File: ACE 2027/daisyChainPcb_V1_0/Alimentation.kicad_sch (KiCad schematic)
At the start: 3 parts, among them U2 AP7361C-33E-13

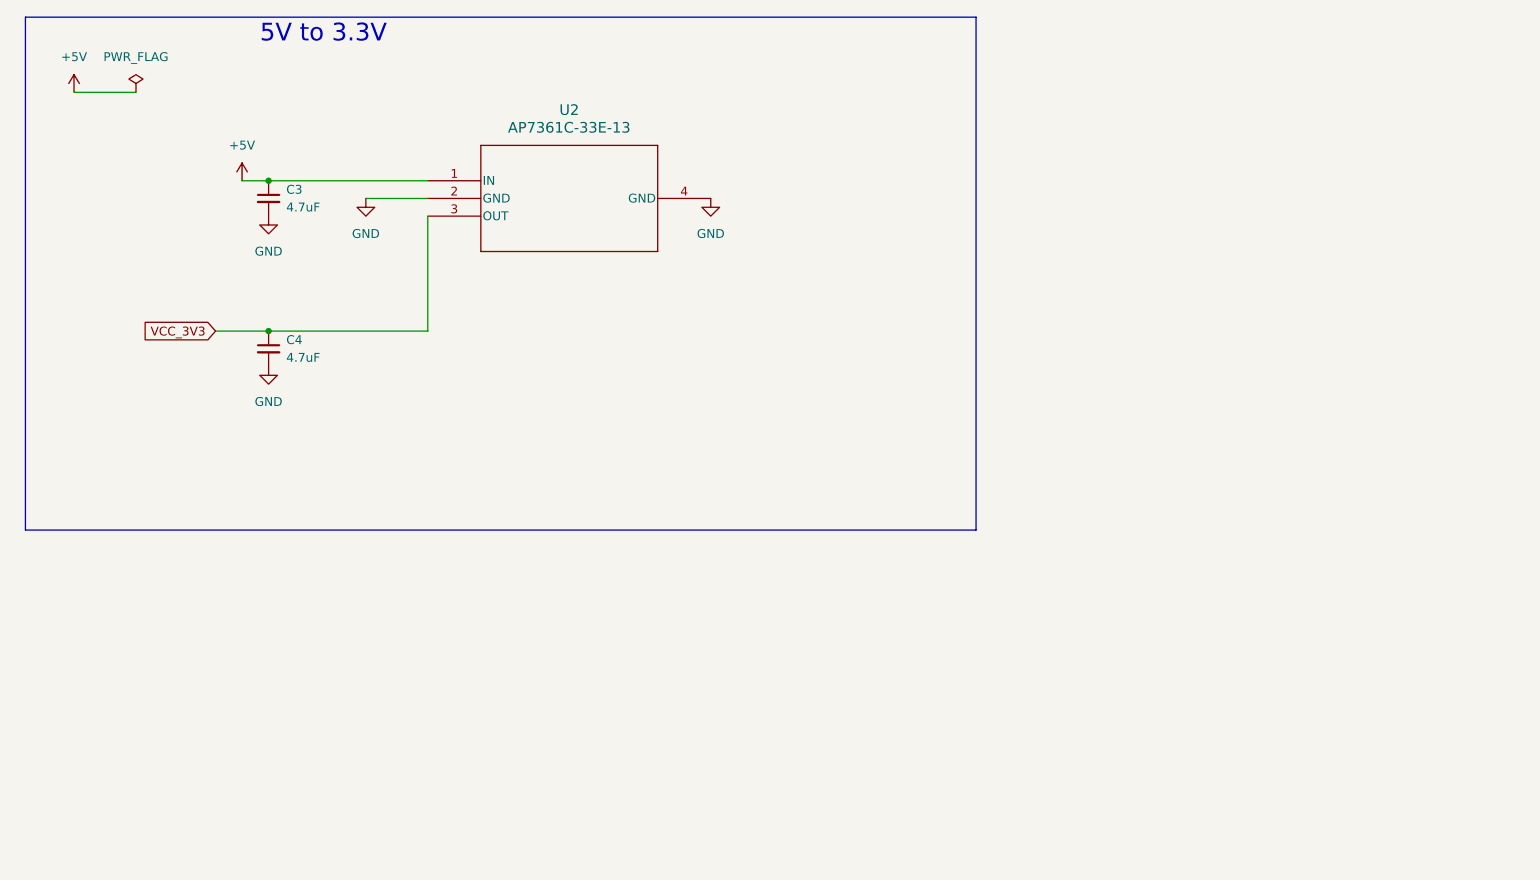
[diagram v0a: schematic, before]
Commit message: Updated grounds to reflect the two grounds we have
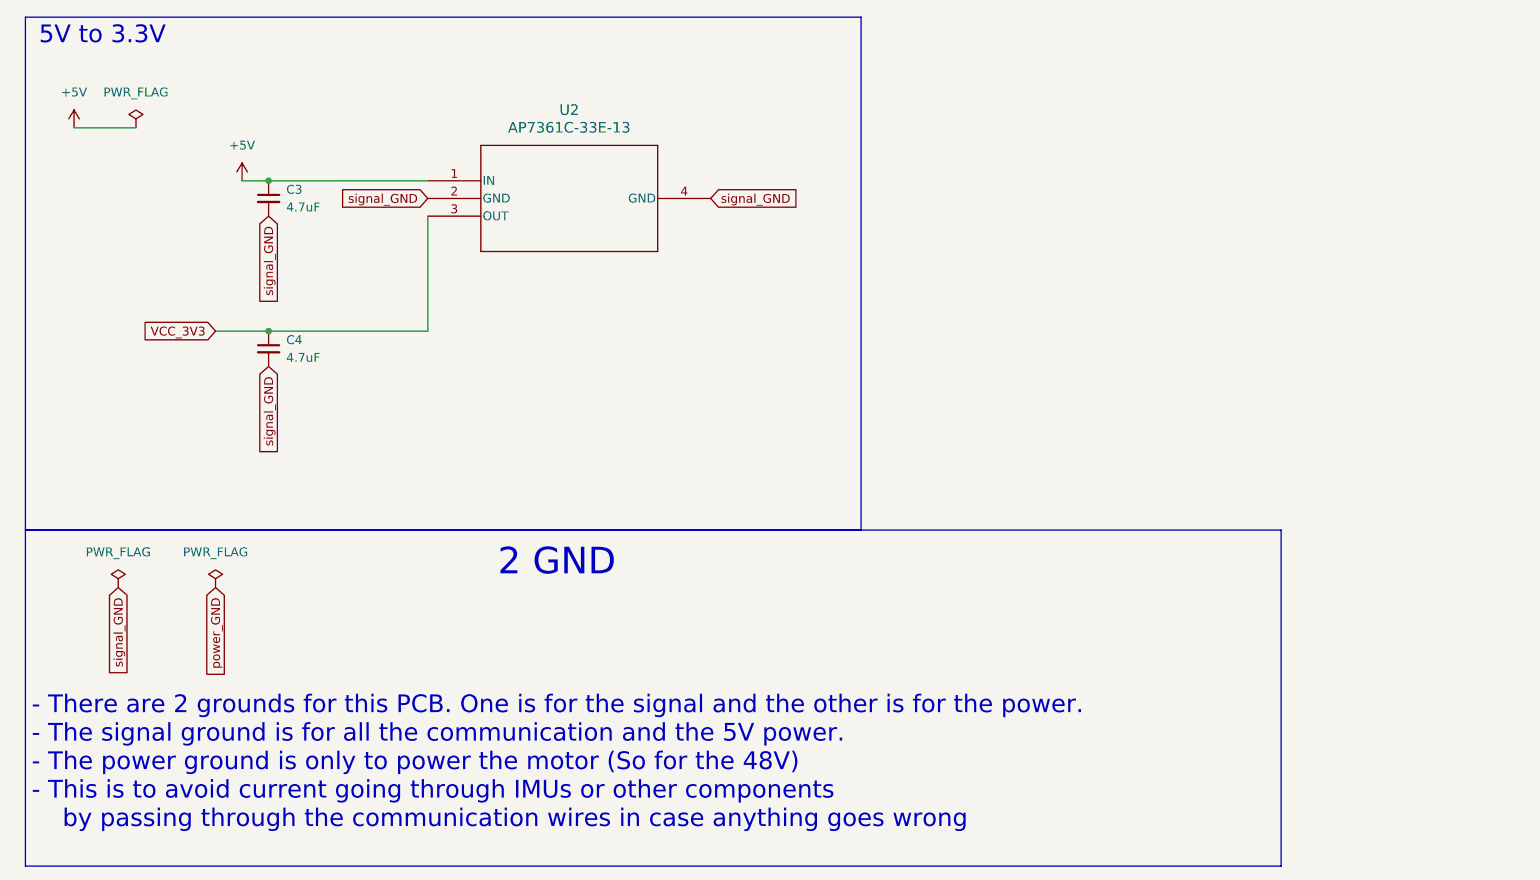
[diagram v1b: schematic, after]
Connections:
- net GND renamed signal_GND
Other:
- note added: "- There are 2 grounds for this PCB. One is for the signal and the other is for the power. - The signal ground is for all the communication and the 5V power. - The power ground is only to power the motor (So for the 48V) - This is to avoid current going through IMUs or other components by passing through the communication wires in case anything goes wrong"
- note added: "2 GND"
